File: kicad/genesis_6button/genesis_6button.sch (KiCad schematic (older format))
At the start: 21 parts, among them J1 Conn_02x07_Odd_Even, J2 DB9_Female, J3 Conn_02x03_Odd_Even, U1 74LS257, U2 ATtiny204-SS, U3 74LS257

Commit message: Change to actual component values + comments
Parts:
- R1, R10, R11, R12, R2, R3, R4, R5, R6, R7, R8, R9: value 47k -> 75k
- U1, U3: value 74LS257 -> 74HC257
- U2: value ATtiny204-SS -> ATtiny404-SS
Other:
- note added: "Add 100k pulldowns to enable\n3-button functionality when\nATTiny404 is missing or blank"
- note added: "Not actually a DB9 connector--just holes for wires."
- note added: "Resistor value is tested working\ndifferent value could be better."
- note added: "To console"
- note added: "To switches\n(ground common, SPST)"
- note added: "UPDI programming header"
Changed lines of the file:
@@
 U 1 1 62FB82B8
 P 5800 2100
-F 0 "U3" H 5350 3100 50  0000 C CNN
-F 1 "74LS257" H 5450 2950 50  0000 C CNN
+F 0 "U3" H 5350 3050 50  0000 C CNN
+F 1 "74HC257" H 5450 2950 50  0000 C CNN
 F 2 "Package_SO:SOIC-16_3.9x9.9mm_P1.27mm" H 5800 2100 50  0001 C CNN
 F 3 "http://www.ti.com/lit/gpn/sn74LS257" H 5800 2100 50  0001 C CNN
@@
 P 2950 2100
 F 0 "U1" H 2350 3000 50  0000 C CNN
-F 1 "74LS257" H 2450 2900 50  0000 C CNN
+F 1 "74HC257" H 2450 2900 50  0000 C CNN
 F 2 "Package_SO:SOIC-16_3.9x9.9mm_P1.27mm" H 2950 2100 50  0001 C CNN
 F 3 "http://www.ti.com/lit/gpn/sn74LS257" H 2950 2100 50  0001 C CNN
@@
 P 3450 5000
 F 0 "U2" H 2800 5850 50  0000 C CNN
-F 1 "ATtiny204-SS" H 3000 5700 50  0000 C CNN
+F 1 "ATtiny404-SS" H 3000 5700 50  0000 C CNN
 F 2 "Package_SO:SOIC-14_3.9x8.7mm_P1.27mm" H 3450 5000 50  0001 C CIN
 F 3 "http://ww1.microchip.com/downloads/en/DeviceDoc/50002687A.pdf" H 3450 5000 50  0001 C CNN
@@
 P 9300 4050
 F 0 "R1" V 9300 4500 50  0000 C CNN
-F 1 "47k" V 9300 4650 50  0000 C CNN
+F 1 "75k" V 9300 4650 50  0000 C CNN
 F 2 "Resistor_SMD:R_0805_2012Metric" V 9230 4050 50  0001 C CNN
 F 3 "~" H 9300 4050 50  0001 C CNN
@@
 P 9300 4200
 F 0 "R2" V 9300 4650 50  0000 C CNN
-F 1 "47k" V 9300 4800 50  0000 C CNN
+F 1 "75k" V 9300 4800 50  0000 C CNN
 F 2 "Resistor_SMD:R_0805_2012Metric" V 9230 4200 50  0001 C CNN
 F 3 "~" H 9300 4200 50  0001 C CNN
@@
 P 9300 4350
 F 0 "R3" V 9300 4800 50  0000 C CNN
-F 1 "47k" V 9300 4950 50  0000 C CNN
+F 1 "75k" V 9300 4950 50  0000 C CNN
 F 2 "Resistor_SMD:R_0805_2012Metric" V 9230 4350 50  0001 C CNN
 F 3 "~" H 9300 4350 50  0001 C CNN
@@
 P 9300 4550
 F 0 "R4" V 9300 5000 50  0000 C CNN
-F 1 "47k" V 9300 5150 50  0000 C CNN
+F 1 "75k" V 9300 5150 50  0000 C CNN
 F 2 "Resistor_SMD:R_0805_2012Metric" V 9230 4550 50  0001 C CNN
 F 3 "~" H 9300 4550 50  0001 C CNN
@@
 P 9300 4700
 F 0 "R5" V 9300 5150 50  0000 C CNN
-F 1 "47k" V 9300 5300 50  0000 C CNN
+F 1 "75k" V 9300 5300 50  0000 C CNN
 F 2 "Resistor_SMD:R_0805_2012Metric" V 9230 4700 50  0001 C CNN
 F 3 "~" H 9300 4700 50  0001 C CNN
@@
 P 9300 4850
 F 0 "R6" V 9300 5300 50  0000 C CNN
-F 1 "47k" V 9300 5450 50  0000 C CNN
+F 1 "75k" V 9300 5450 50  0000 C CNN
 F 2 "Resistor_SMD:R_0805_2012Metric" V 9230 4850 50  0001 C CNN
 F 3 "~" H 9300 4850 50  0001 C CNN
@@
 P 9300 5050
 F 0 "R7" V 9300 5500 50  0000 C CNN
-F 1 "47k" V 9300 5650 50  0000 C CNN
+F 1 "75k" V 9300 5650 50  0000 C CNN
 F 2 "Resistor_SMD:R_0805_2012Metric" V 9230 5050 50  0001 C CNN
 F 3 "~" H 9300 5050 50  0001 C CNN
@@
 P 9300 5200
 F 0 "R8" V 9300 5650 50  0000 C CNN
-F 1 "47k" V 9300 5800 50  0000 C CNN
+F 1 "75k" V 9300 5800 50  0000 C CNN
 F 2 "Resistor_SMD:R_0805_2012Metric" V 9230 5200 50  0001 C CNN
 F 3 "~" H 9300 5200 50  0001 C CNN
@@
 P 9300 5350
 F 0 "R9" V 9300 5800 50  0000 C CNN
-F 1 "47k" V 9300 5950 50  0000 C CNN
+F 1 "75k" V 9300 5950 50  0000 C CNN
 F 2 "Resistor_SMD:R_0805_2012Metric" V 9230 5350 50  0001 C CNN
 F 3 "~" H 9300 5350 50  0001 C CNN
@@
 P 9300 5500
 F 0 "R10" V 9300 5950 50  0000 C CNN
-F 1 "47k" V 9300 6100 50  0000 C CNN
+F 1 "75k" V 9300 6100 50  0000 C CNN
 F 2 "Resistor_SMD:R_0805_2012Metric" V 9230 5500 50  0001 C CNN
 F 3 "~" H 9300 5500 50  0001 C CNN
@@
 P 9300 5700
 F 0 "R11" V 9300 6150 50  0000 C CNN
-F 1 "47k" V 9300 6300 50  0000 C CNN
+F 1 "75k" V 9300 6300 50  0000 C CNN
 F 2 "Resistor_SMD:R_0805_2012Metric" V 9230 5700 50  0001 C CNN
 F 3 "~" H 9300 5700 50  0001 C CNN
@@
 P 9300 5850
 F 0 "R12" V 9300 6300 50  0000 C CNN
-F 1 "47k" V 9300 6450 50  0000 C CNN
+F 1 "75k" V 9300 6450 50  0000 C CNN
 F 2 "Resistor_SMD:R_0805_2012Metric" V 9230 5850 50  0001 C CNN
 F 3 "~" H 9300 5850 50  0001 C CNN
@@
 Wire Wire Line
 	4550 6400 4850 6400
+Text Notes 7650 2950 0    50   ~ 0
+Not actually a DB9 connector--just holes for wires.
+Text Notes 4700 6050 0    50   ~ 0
+UPDI programming header
+Text Notes 8150 3850 0    50   ~ 0
+Resistor value is tested working\ndifferent value could be better.
+Text Notes 5050 4050 0    50   ~ 0
+Add 100k pulldowns to enable\n3-button functionality when\nATTiny404 is missing or blank
+Text Notes 8600 1250 0    50   ~ 0
+To console
+Text Notes 6050 4550 0    50   ~ 0
+To switches\n(ground common, SPST)
 $EndSCHEMATC

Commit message: Second PCB iteration (untested)
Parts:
- added C4: 10u, Capacitor_THT:CP_Radial_D8.0mm_P5.00mm, symbol Device:CP
- added R13, R14: 100k, Resistor_SMD:R_0805_2012Metric, symbol Device:R
- added TP1, TP2: TestPoint, TestPoint:TestPoint_Loop_D3.50mm_Drill0.9mm_Beaded, symbol Connector:TestPoint
- C1, C2, C3: footprint Capacitor_SMD:C_0805_2012Metric -> Capacitor_SMD:C_1206_3216Metric
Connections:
- net +5V: now also C4.1, TP1.1
- net BUTTON_DOWN: now also U3.2 (I0a); no longer U3.5 (I0b)
- net BUTTON_MODE: now also U2.3 (PA5)
- net BUTTON_UP: now also U3.5 (I0b); no longer U3.2 (I0a)
- net BUTTON_Y: now also U3.3 (I1a); no longer U3.6 (I1b)
- net BUTTON_Z: now also U3.6 (I1b); no longer U3.3 (I1a)
- net DOWN: now also U3.4 (Za); no longer U3.7 (Zb)
- net GND: now also C4.2, R13.1, R14.1, TP2.1
- net UP: now also U3.7 (Zb); no longer U3.4 (Za)
- net at U2.2 (PA4), U3.1 (S): now also R13.2
- net at U2.5 (PA7), U3.15 (OE): now also R14.2
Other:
- moved on the sheet: C2, U2

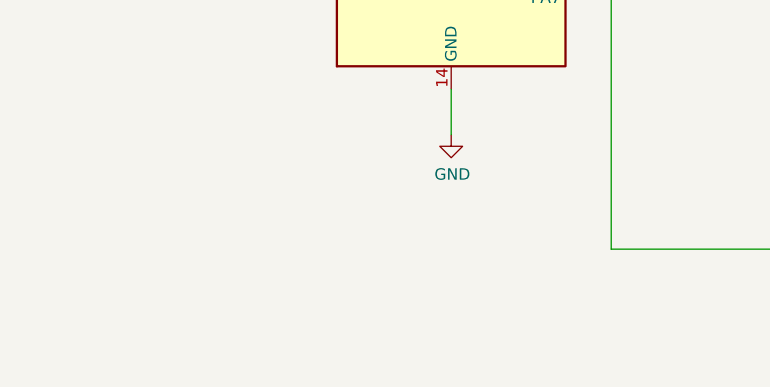
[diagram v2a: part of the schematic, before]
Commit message: Add hole for cable tie + replace/route
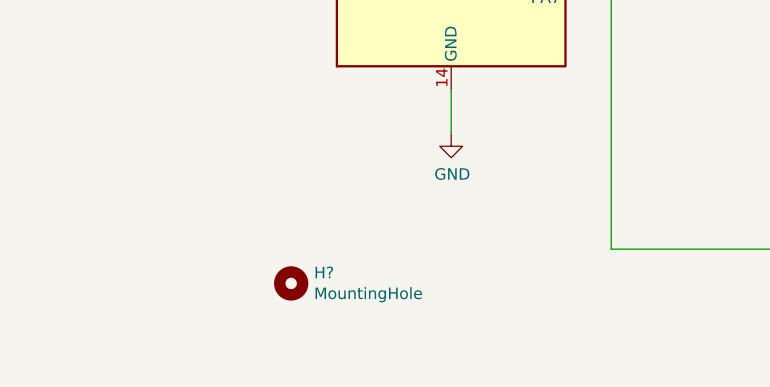
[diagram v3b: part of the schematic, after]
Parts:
- added H?: MountingHole, MountingHole:MountingHole_5.3mm_M5, symbol Mechanical:MountingHole
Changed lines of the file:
@@
 Wire Wire Line
 	10150 2000 10150 2100
+$Comp
+L Mechanical:MountingHole H?
+U 1 1 630E5D91
+P 2300 6550
+F 0 "H?" H 2400 6596 50  0000 L CNN
+F 1 "MountingHole" H 2400 6505 50  0000 L CNN
+F 2 "MountingHole:MountingHole_5.3mm_M5" H 2300 6550 50  0001 C CNN
+F 3 "~" H 2300 6550 50  0001 C CNN
+	1    2300 6550
+	1    0    0    -1
+$EndComp
 $EndSCHEMATC

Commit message: Re-annotate and update pcb
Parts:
- gave numbers to parts that had none: 1
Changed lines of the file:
@@
 	10150 2000 10150 2100
 $Comp
-L Mechanical:MountingHole H?
+L Mechanical:MountingHole H1
 U 1 1 630E5D91
 P 2300 6550
-F 0 "H?" H 2400 6596 50  0000 L CNN
+F 0 "H1" H 2400 6596 50  0000 L CNN
 F 1 "MountingHole" H 2400 6505 50  0000 L CNN
 F 2 "MountingHole:MountingHole_5.3mm_M5" H 2300 6550 50  0001 C CNN
